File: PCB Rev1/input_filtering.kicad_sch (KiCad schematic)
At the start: 13 parts

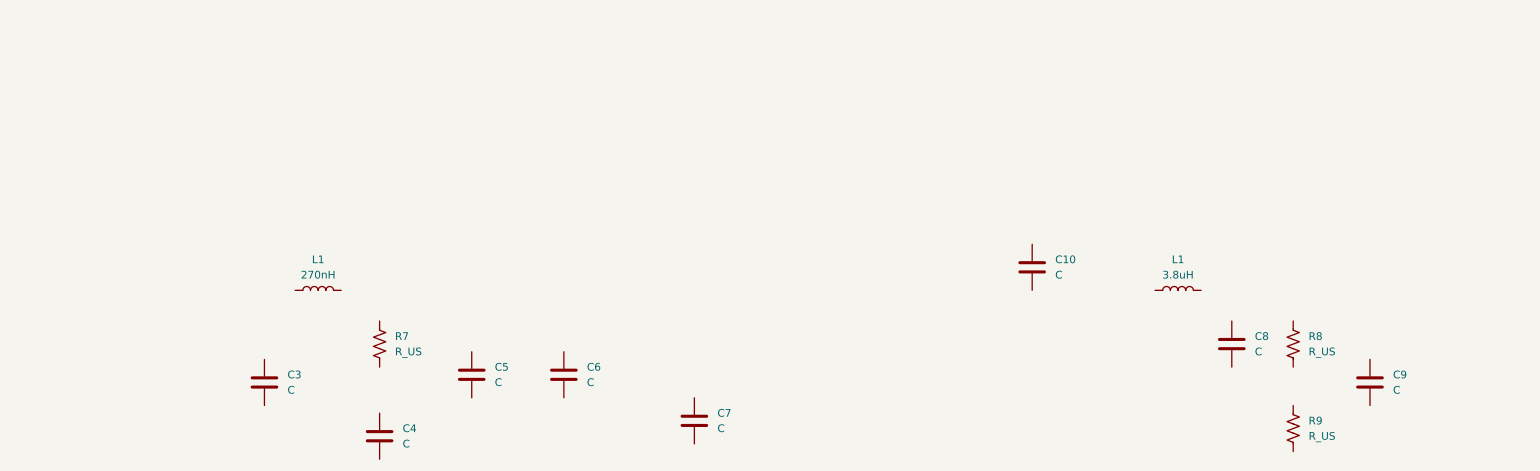
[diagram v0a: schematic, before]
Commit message: Added power filtering stage 1, DC->DC Buck
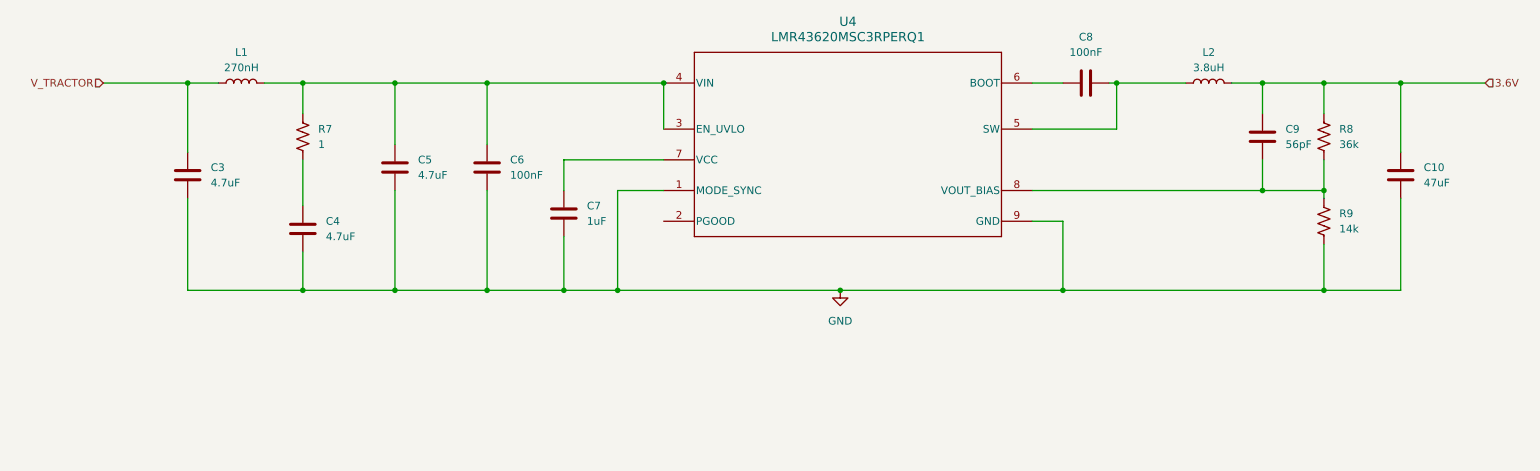
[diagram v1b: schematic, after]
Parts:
- added U4: LMR43620MSC3RPERQ1, RPE0009A-MFG, symbol buck_conv:LMR43620MSC3RPERQ1
- C10: renamed from C9; value C -> 47uF
- C3, C4, C5: value C -> 4.7uF
- C6: value C -> 100nF
- C7: value C -> 1uF
- C8: renamed from C10; value C -> 100nF
- C9: renamed from C8; value C -> 56pF
- R7: value R_US -> 1
- R8: value R_US -> 36k
- R9: value R_US -> 14k
- renumbered L1 to L2
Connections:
- net 3.6V: now reaches C9.1
- net 3.6V: now also C10.1, L2.2, R8.2
- net at C9.2: now also R8.1, R9.2, U4.8 (VOUT_BIAS)
- net GND: now reaches R9.1
- net GND: now also C10.2, C3.2, C4.2, C5.2, C6.2, C7.2, U4.1 (MODE_SYNC), U4.9 (GND)
- net at R7.1: now also C4.1
- net at R7.2: now also C5.1, C6.1, L1.2, U4.3 (EN_UVLO), U4.4 (VIN)
- net at C8.1: now also U4.6 (BOOT)
- net at C8.2: now also L2.1, U4.5 (SW)
- net V_TRACTOR: now reaches L1.1
- net V_TRACTOR: now also C3.1
- net at C7.1: now also U4.7 (VCC)
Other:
- moved on the sheet: C10, C3, C4, C5, C6, C7, C8, C9, L1, L2, R7, R8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

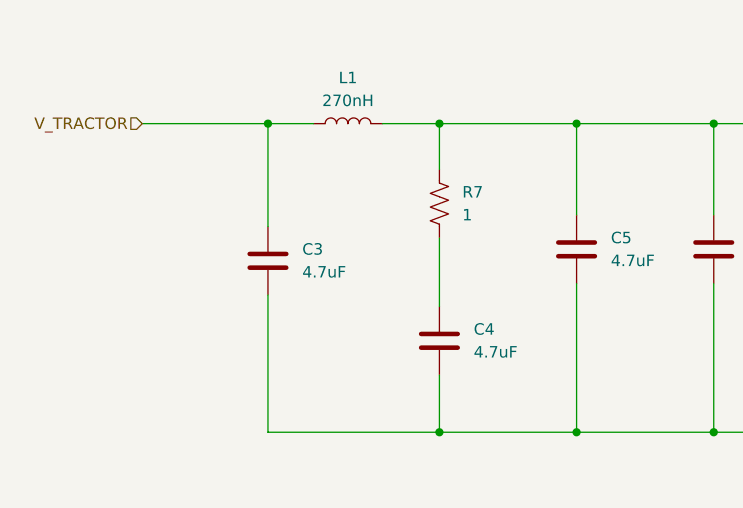
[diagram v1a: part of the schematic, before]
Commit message: Starting work on power tree, introduced power mux
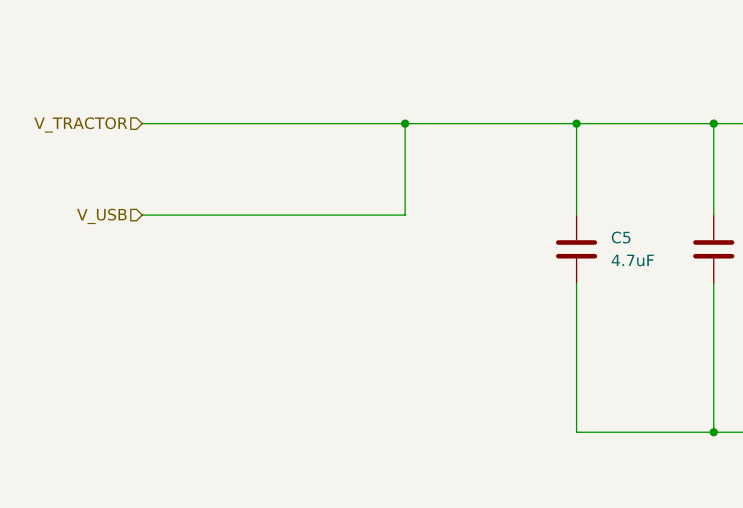
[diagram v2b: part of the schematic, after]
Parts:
- removed C3, C4: 4.7uF, symbol Device:C
- removed L1: 270nH, symbol Device:L
- removed R7: 1, symbol Device:R_US
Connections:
- net V_TRACTOR: now also C5.1, C6.1, U4.3 (EN_UVLO), U4.4 (VIN)

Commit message: Progress marches on.
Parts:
- U4: footprint RPE0009A-MFG -> footprints:RPE0009A-MFG
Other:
- note added: "add in the TVS diode"
- note added: "add in the schottkey diode"
- note added: "todo: source footprints and 3D models for components."
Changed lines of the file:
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@@
 	(generator_version "9.0")
 	(paper "A4")
+	(text "add in the schottkey diode\n"
+		(exclude_from_sim no)
+		(at 70.612 104.648 0)
+		(effects
+			(font
+				(size 1.27 1.27)
+			)
+		)
+	)
+	(text "todo: source footprints and 3D models for components."
+		(exclude_from_sim no)
+		(at 78.74 100.076 0)
+		(effects
+			(font
+				(size 1.27 1.27)
+			)
+		)
+	)
+	(text "add in the TVS diode"
+		(exclude_from_sim no)
+		(at 67.818 108.966 0)
+		(effects
+			(font
+				(size 1.27 1.27)
+			)
+		)
+	)
 	(junction
 		(at 194.31 85.09)
@@
 			)
 		)
-		(property "Footprint" "RPE0009A-MFG"
+		(property "Footprint" "footprints:RPE0009A-MFG"
 			(at 128.27 50.8 0)
 			(effects

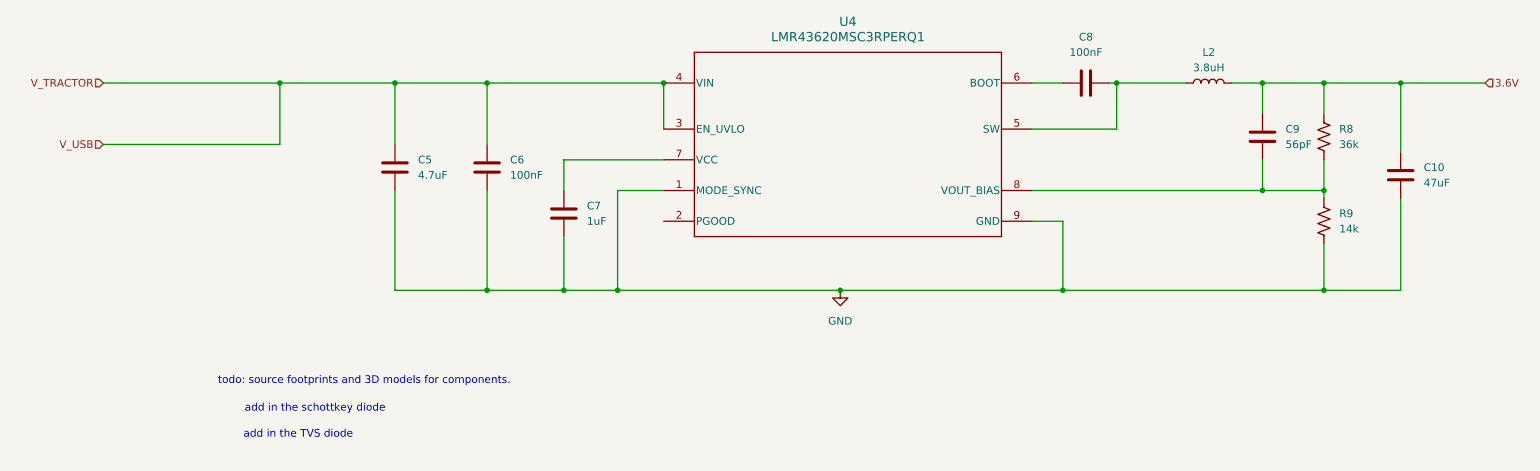
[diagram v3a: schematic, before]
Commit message: aggregated SD card and switch, updated power architecture to use 5V, added TVS diode array
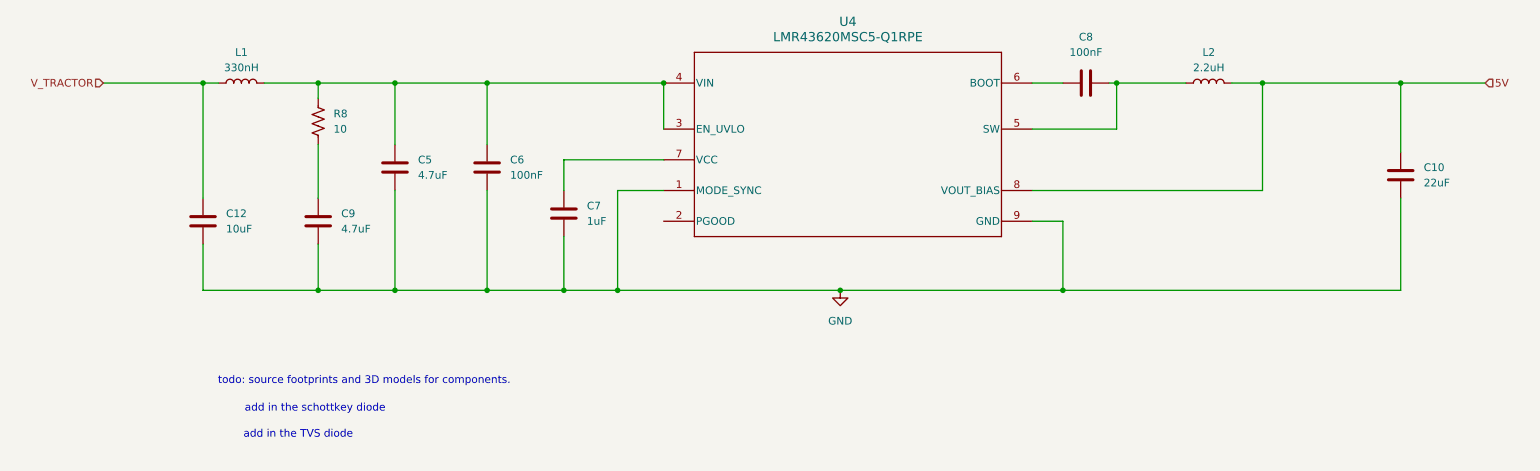
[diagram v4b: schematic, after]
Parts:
- removed R9: 14k, symbol Device:R_US
- added C12: 10uF, symbol Device:C
- added L1: 330nH, symbol Device:L
- C10: value 47uF -> 22uF
- C9: value 56pF -> 4.7uF
- L2: value 3.8uH -> 2.2uH
- R8: value 36k -> 10
- U4: value LMR43620MSC3RPERQ1 -> LMR43620MSC5-Q1RPE; footprint footprints:RPE0009A-MFG -> (none)
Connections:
- net GND: now also C9.2, C12.2
- net V_TRACTOR: now also C12.1, L1.1; no longer C5.1, C6.1, U4.3 (EN_UVLO), U4.4 (VIN)
- net 3.6V: no longer names the net of C9.1, R8.2
- net 3.6V: no longer C10.1, L2.2
- new net: C5.1, C6.1, L1.2, R8.1, U4.3 (EN_UVLO), U4.4 (VIN)
- new net 5V: C10.1, L2.2, U4.8 (VOUT_BIAS)

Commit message: hey now, over under 5 more hours of work?
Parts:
- U4: footprint (none) -> footprints:RPE0009A-MFG
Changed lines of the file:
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@@
 			)
 		)
-		(property "Footprint" ""
+		(property "Footprint" "footprints:RPE0009A-MFG"
 			(at 128.27 50.8 0)
 			(effects

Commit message: added new files and switches, notes,tps
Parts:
- renumbered C12 to C1, C9 to C2, C5 to C3, C6 to C4, C7 to C5, C8 to C6, C10 to C7, R8 to R2, U4 to U3
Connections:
- no-connect marks 0 -> 1
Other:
- note added: "find 50V rated good quality x7 ceramic caps"
- note removed: "add in the TVS diode"
- company: (none) -> California Strawberry Commission
- title: (none) -> 12V Switching Regulator

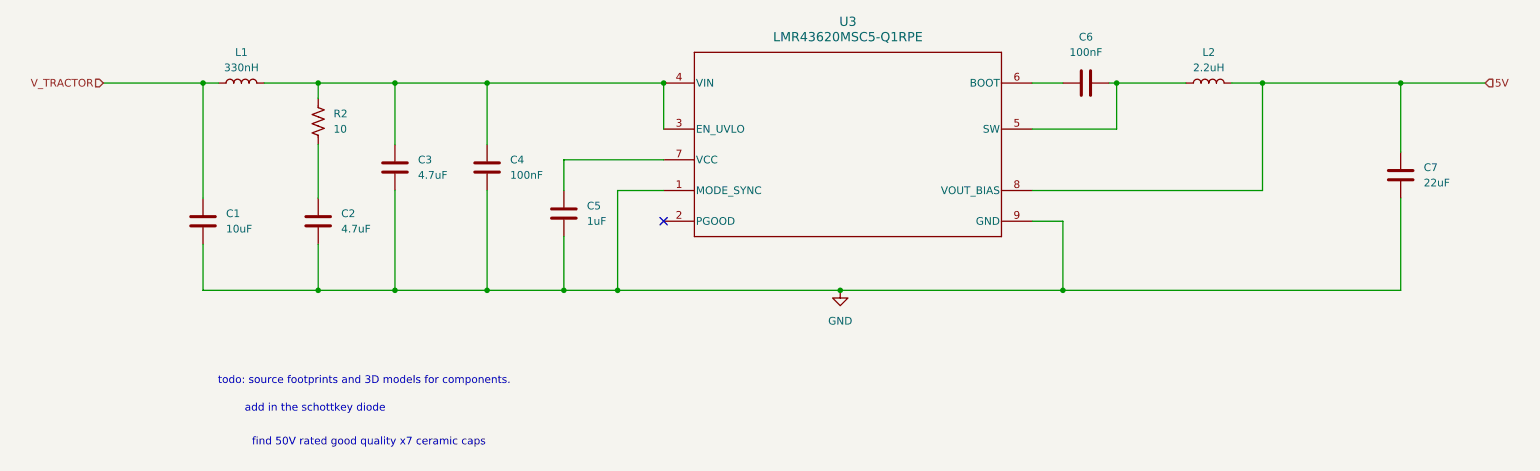
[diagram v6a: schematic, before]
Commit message: rev 2 schematic with minor changes, final send out before layout
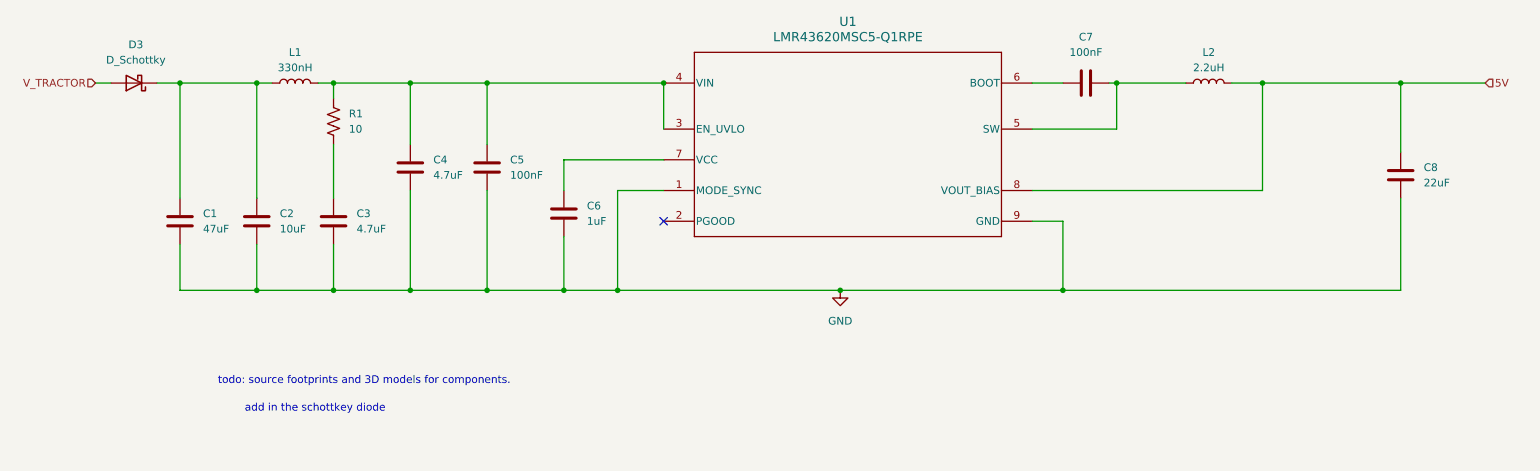
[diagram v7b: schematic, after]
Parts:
- added C1: 47uF, symbol Device:C
- added D3: D_Schottky, symbol Device:D_Schottky
- L2: footprint (none) -> Inductor_SMD:L_TDK_VLS6045EX_VLS6045AF; Part # (none) -> VLS6045EX-2R2N
- renumbered C1 to C2, C2 to C3, C3 to C4, C4 to C5, C5 to C6, C6 to C7, C7 to C8, R2 to R1, U3 to U1
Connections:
- net GND: now also C1.2
- net V_TRACTOR: now also D3.2 (A); no longer C2.1, L1.1
- new net: C1.1, C2.1, D3.1 (K), L1.1
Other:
- note removed: "find 50V rated good quality x7 ceramic caps"
- moved on the sheet: C2, C3, C4, L1, R1

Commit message: added PCB rev2!
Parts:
- removed C1: 47uF, symbol Device:C
- C1: renamed from C2; footprint (none) -> footprints:CAPC3216X190N; Part # (none) -> CGA5L1X7R1H106K160AE
- C2: renamed from C3; footprint (none) -> footprints:CAPC2012X150N; Part # (none) -> CGA4J1X7R1H475K125AC
- C3: renamed from C4; footprint (none) -> footprints:CAPC2012X150N; Part # (none) -> CGA4J1X7R1H475K125AC
- C4: renamed from C5; footprint (none) -> footprints:CAPC2012X94N; Part # (none) -> 08055C104K4Z2A
- C5: renamed from C6; footprint (none) -> Capacitor_SMD:C_0805_2012Metric; Part # (none) -> UMK212B7105KGHT
- C6: renamed from C7; footprint (none) -> footprints:CAPC1005X55N; Part # (none) -> LMK105B7104KVHF
- C7: renamed from C8; footprint (none) -> footprints:CAPC3216X190N; Part # (none) -> LMJ316BB7226KLHT
- D3: footprint (none) -> footprints:CR_SMP_DO-220AA_VIS; Part # (none) -> SS2PH5HM3-84A
- L1: footprint (none) -> footprints:WE-MAPI_2510; Part # (none) -> 744383230033
- R1: footprint (none) -> footprints:RES_ERJ3EKF10R0V; Part # (none) -> ERJ-3EKF10R0V
- U1: Part # (none) -> LMR43620MSC5-Q1RPE
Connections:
- net V_TRACTOR: now also D3.1 (K); no longer D3.2 (A)
- net V_IN_BUCK: now reaches C3.1, C4.1, L1.2, R1.1, U1.3 (EN_UVLO), U1.4 (VIN)
- net PI_IN: now reaches C1.1, L1.1
- net PI_IN: now also D3.2 (A); no longer D3.1 (K)
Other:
- note removed: "add in the schottkey diode"
- note removed: "todo: source footprints and 3D models for components."
- moved on the sheet: D3
